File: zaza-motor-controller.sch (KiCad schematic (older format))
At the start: 74 parts, among them J1 VIN, J2 VIN, J3 CONN_02X05, J4 CONN_02X01, J5 GS3, Q1 3904, Q10 3906, Q11 3904, Q12 3904, Q2 3904, Q3 3906, Q4 3904, Q5 IXTA220, Q6 IXTA220, Q7 IXTA220, Q8 IXTA220, Q9 3904, U1 74HC00, U2 74HC00, U3 LM358, U4 LM555N

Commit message: Rev1 dev
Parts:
- removed D11, D12: BAT5H17, Diodes_SMD:D_MiniMELF_Standard, symbol D_Schottky_Small_ALT
- removed Q10: 3906, TO_SOT_Packages_SMD:SOT-23, symbol Q_PNP_BEC
- removed Q11, Q12, Q9: 3904, TO_SOT_Packages_SMD:SOT-23, symbol Q_NPN_BEC
- removed R10, R11, R13, R14: 10k, Resistors_SMD:R_0805, symbol R_Small
- removed R12: 47k, Resistors_SMD:R_0805, symbol R_Small
- removed R23: 3.3k, Resistors_SMD:R_0805, symbol R_Small
- added C15: CP, Capacitors_THT:CP_Axial_L29.0mm_D20.0mm_P35.00mm_Horizontal, symbol CP
- added C?: 220n, symbol C_Small
- added D? (x2): 15.6V, symbol D_Zener_Small_ALT
- added D? (x2): D, symbol D_Small_ALT
- added J?: MX120G, symbol CONN_02X06
- added MX120G: CONN_01X12, symbol CONN_01X12
- added Q?: Q_NPN_BCE, symbol Q_NPN_BCE
- added R? (x2): 10k, symbol R_Small
- added R?: 50R, symbol R_Small
- added R?: 10k, Resistors_SMD:R_0805, symbol R_Small
- added R? (x2): 1k, symbol R_Small
- added U?: 74xx595, symbol 74xx595
- added U?: 74xx138, symbol 74xx138
- added U?: LM7805CT, TO_SOT_Packages_THT:TO-220_Vertical, symbol LM7805CT
- added U?: IRS2003, symbol IRS2003
- Q1, Q2, Q4: value 3904 -> BC337
- Q3: value 3906 -> BC327
- R21: value 200k -> 180k
- R6: value 10k -> 100k
- R7: value 47k -> 0R
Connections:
- net +48V: now also R8.2, C15.1, MX120G.1 (P1), R?.1, R?.2; no longer Q3.3 (C), R8.1
- net +5V: now also U?.10 (R), U?.16, U?.16 (VCC), U?.6
- net GND: now also D?.2 (A), U?.13 (EN3), U?.2 (GND), U?.4, U?.5, U?.8, U?.8
- net GNDPWR: now also C15.2, MX120G.2 (P2), U?.4 (COM)
- net M+: now also R?.2
- net M-: now also C?.2, D?.2 (A), U?.6 (VS)
- net U: now also U?.15
- net V: now also U?.1
- net ~A: no longer R4.1
- net ~B: no longer R5.1
- net ~D: now also U?.2 (HIN)
- net at D10.1 (K), Q4.3 (C), Q6.1 (G)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: now also R8.1; no longer R8.2
- net at Q7.1 (G): now also R?.2
- net at Q8.1 (G): now also R?.2
- new net: Q3.3 (C), R?.1
- new net: D?.1 (K), Q?.1 (B), R?.1
- new net: Q?.2 (C), R?.2, R?.2
- new net: Q?.3 (E), U?.1 (IN)
- new net: R?.1, U?.5 (LO)
- new net: R?.1, U?.7 (HO)
- new net: C?.1, D?.1 (K), D?.1 (K), D?.1 (K), U?.8 (VB)
- new net: D?.2 (A), R?.1
- new net +15V: D?.2 (A), U?.1 (VCC)
- new net CS_ADDR0: MX120G.8 (P8), U?.1 (0)
- new net CS_ADDR1: MX120G.9 (P9), U?.2
- new net CS_ADDR2: MX120G.10 (P10), U?.3 (2)
- new net GNDREF: MX120G.4 (P4)
- new net MISO: MX120G.6 (P6)
- new net MOSI: MX120G.5 (P5), U?.14
- new net SCLK: MX120G.7 (P7), U?.11 (C1/->)
- new net ~CS_ADC: U?.13 (2)
- new net ~CS_DAC: U?.12 (3)
- new net ~CS_GPO: U?.12 (C2), U?.14 (1)
- no-connect marks 2 -> 15
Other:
- note added: "1\n1\n1\n1\n0"
- note added: "330mV/A"
- note added: "r_m = 10mV/A"
- note removed: "0\n0\n0\n0\n1"
- note removed: "V = 330mV/A"
- note removed: "rm = 10mV/A"
- moved on the sheet: C1, C10, C11, C12, C13, C14, C2, C3, C4, C5, C6, C7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

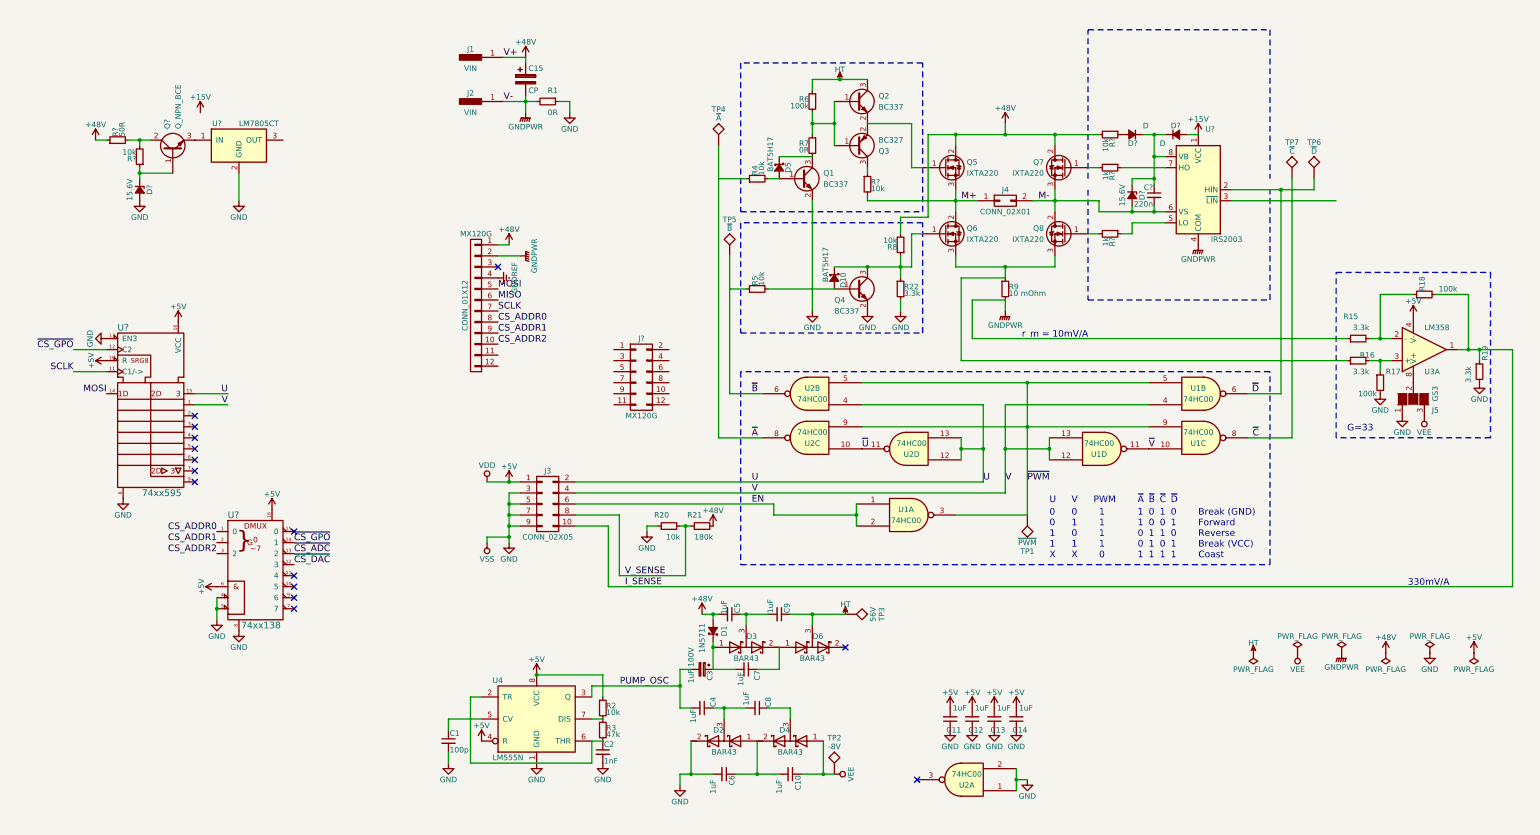
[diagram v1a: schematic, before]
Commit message: schematic: Getting closer to rev 1
Replace dscrete FET driver with IRS2003.
Add ADC, and other cool shit.
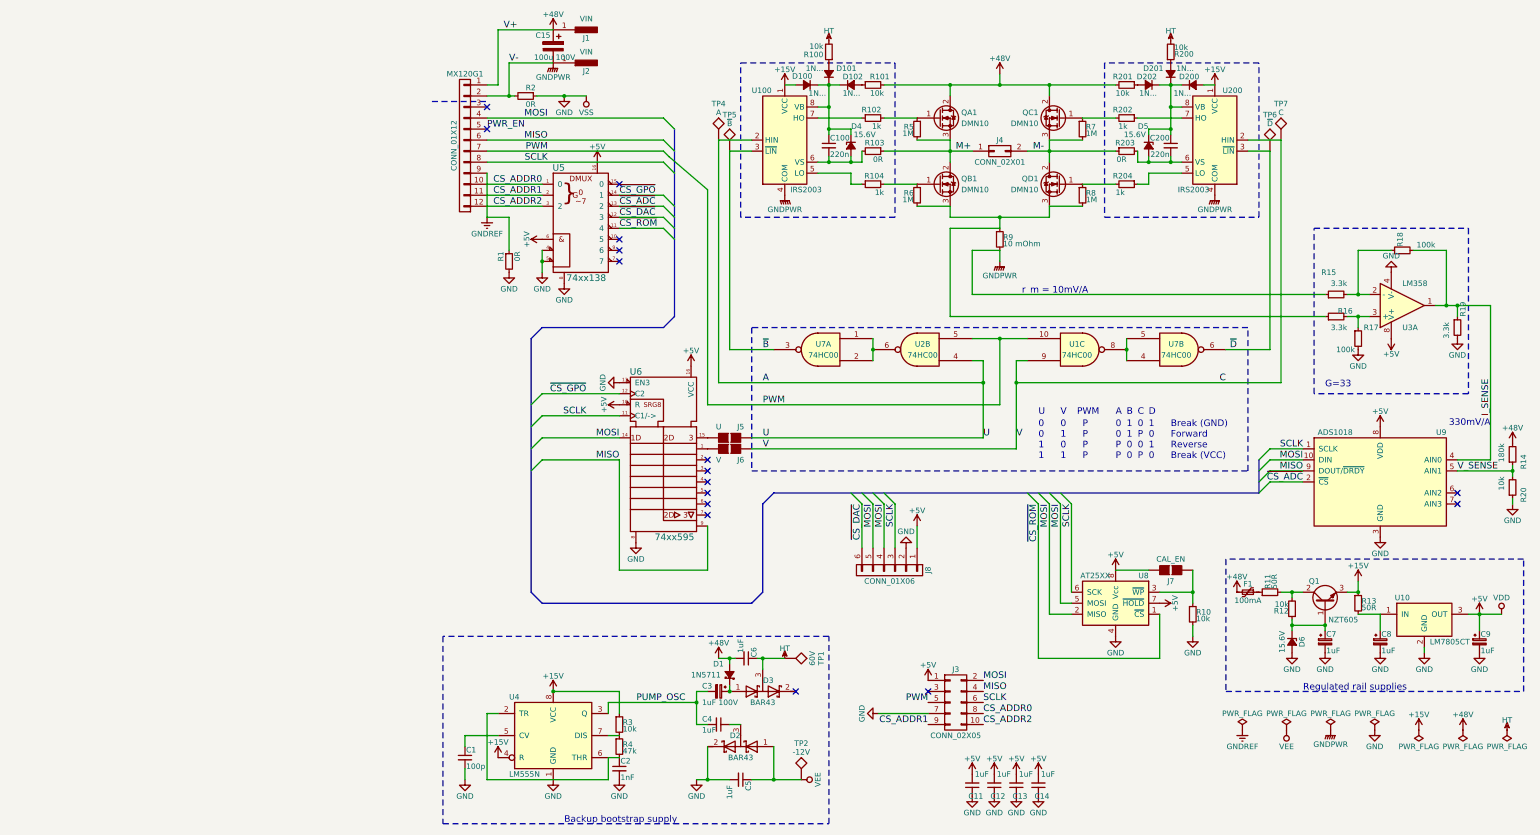
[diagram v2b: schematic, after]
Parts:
- removed C10, C7, C8, C9: 1uF, Capacitors_SMD:C_0805, symbol C_Small
- removed C?: 220n, symbol C_Small
- removed D10, D5: BAT5H17, Diodes_SMD:D_MiniMELF_Standard, symbol D_Schottky_Small_ALT
- removed D4, D6: BAR43, TO_SOT_Packages_SMD:SOT-23, symbol D_Schottky_x2_Serial_AKC
- removed D? (x2): D, symbol D_Small_ALT
- removed D?: 15.6V, symbol D_Zener_Small_ALT
- removed J5: GS3, Connectors:GS3, symbol GS3
- removed J?: MX120G, symbol CONN_02X06
- removed MX120G: CONN_01X12, symbol CONN_01X12
- removed Q1, Q2, Q4: BC337, TO_SOT_Packages_SMD:SOT-23, symbol Q_NPN_BEC
- removed Q3: BC327, TO_SOT_Packages_SMD:SOT-23, symbol Q_PNP_BEC
- removed R21: 180k, Resistors_SMD:R_0805, symbol R_Small
- removed R22: 3.3k, Resistors_SMD:R_0805, symbol R_Small
- removed R?: 10k, Resistors_SMD:R_0805, symbol R_Small
- removed R? (x2): 1k, symbol R_Small
- removed R?: 10k, symbol R_Small
- removed TP3: 56V, Measurement_Points:Test_Point_Keystone_5000-5004_Miniature, symbol TEST
- removed unit 3 of U1
- removed unit 4 of U1
- removed unit 1 of U1
- removed unit 3 of U2
- removed unit 4 of U2
- removed unit 1 of U2
- removed U?: IRS2003, symbol IRS2003
- added C100, C200: 220n, symbol C_Small
- added C7, C8, C9: 1uF, symbol CP_Small
- added D100, D101, D102, D200, D201, D202: 1N..., symbol D_Small_ALT
- added D4, D5: 15.6V, symbol D_Zener_Small_ALT
- added F1: 100mA, symbol Polyfuse_Small
- added J5: U, Connectors:GS2, symbol GS2
- added J6: V, Connectors:GS2, symbol GS2
- added J7: CAL_EN, Connectors:GS2, symbol GS2
- added J8: CONN_01X06, symbol CONN_01X06
- added MX120G1: CONN_01X12, symbol CONN_01X12
- added R10, R100, R101, R200, R201: 10k, symbol R_Small
- added R102, R104, R202, R204: 1k, symbol R_Small
- added R103, R203: 0R, symbol R_Small
- added R13: 50R, symbol R_Small
- added R14: 180k, Resistors_SMD:R_0805, symbol R_Small
- added U100, U200: IRS2003, symbol IRS2003
- added U7: 74HC00, Housings_SOIC:SOIC-14_3.9x8.7mm_Pitch1.27mm, symbol 74xx132
- added U8: AT25XX, symbol AT25_EEPROM
- added U9: ADS1018, symbol ADS1118I
- C15: value CP -> 100u 100V
- Q1: renamed from Q?; value Q_NPN_BCE -> NZT605
- QA1: renamed from Q5; value IXTA220 -> DMN10
- QB1: renamed from Q6; value IXTA220 -> DMN10
- QC1: renamed from Q7; value IXTA220 -> DMN10
- QD1: renamed from Q8; value IXTA220 -> DMN10
- R1: footprint Resistors_SMD:R_0805 -> (none)
- R2: value 10k -> 0R; footprint Resistors_SMD:R_0805 -> (none)
- R3: value 47k -> 10k
- R4: value 10k -> 47k
- R5, R8: value 10k -> 1M; footprint Resistors_SMD:R_0805 -> (none)
- R6: value 100k -> 1M; footprint Resistors_SMD:R_0805 -> (none)
- R7: value 0R -> 1M; footprint Resistors_SMD:R_0805 -> (none)
- TP1: value ~PWM -> 60V
- TP2: value -8V -> -12V
- TP4: value ~A -> A
- TP7: value ~C -> C
- gave numbers to parts that had none: 6
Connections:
- net EN is gone; now on net SCLK: J3.6 (P6)
- net +15V: now also Q1.3 (E), R3.1, U4.4 (R), U4.8 (VCC), D100.2 (A), D200.2 (A), R13.1, U100.1 (VCC), U200.1 (VCC)
- net +48V: now also C6.2, F1.2, MX120G1.1 (P1), R101.2, R14.2, R201.2; no longer C5.2, R11.1, R8.2
- net +5V: now also U10.3 (OUT), U3.8 (V+), C9.1, J7.1 (G1), J8.1 (P1), U7.14 (VDD), U7.14 (VDD), U8.7 (~HOLD), U8.8 (Vcc), U9.8 (VDD); no longer R2.1, U3.4 (V-), U4.4 (R), U4.8 (VCC)
- net CS_ADDR0: now also J3.8 (P8), MX120G1.10 (P10)
- net CS_ADDR1: now also J3.9 (P9), MX120G1.11 (P11)
- net CS_ADDR2: now also J3.10 (P10), MX120G1.12 (P12)
- net GND: now also C5.2, R1.2, R2.1, U3.4 (V-), C7.2, C8.2, C9.2, J8.2 (P2), R10.2, U7.7 (VSS), U7.7 (VSS), U8.4 (GND), U9.3 (GND); no longer C6.2, J3.3 (P3), J3.5 (P5), J3.9 (P9), R1.1
- net GNDPWR: now also R2.2, MX120G1.2 (P2), U100.4 (COM), U200.4 (COM); no longer R1.2
- net GNDREF: now also R1.1, MX120G1.9 (P9)
- net HT: now also C6.1, D3.3 (common), TP1.1, R100.2, R200.2; no longer R6.1
- net I_SENSE: now also U9.4 (AIN0); no longer J3.10 (P10)
- net M+: now also R5.2, R103.1
- net M-: now also R7.2, R203.1
- net MISO: now also J3.4 (P4), U6.9, MX120G1.6 (P6), U9.9 (DOUT/~DRDY)
- net MOSI: now also J3.2 (P2), J8.4 (P4), J8.5 (P5), MX120G1.4 (P4), U8.2 (MISO), U8.5 (MOSI), U9.10 (DIN)
- net SCLK: now also J8.3 (P3), MX120G1.8 (P8), U8.6 (SCK), U9.1 (SCLK)
- net VEE: now also C5.1, D2.1 (A)
- net V_SENSE: now also R14.1, U9.5 (AIN1); no longer J3.8 (P8)
- net ~B: now also U100.3 (~LIN), U7.3; no longer U2.6
- net ~CS_ADC: now also U9.2 (~CS)
- net ~CS_DAC: now also J8.6 (P6)
- net ~D: now also U200.3 (~LIN), U7.6; no longer U1.6
- net at QA1.1 (G): now also R5.1, R102.2
- net at QB1.1 (G): now also R6.1, R104.2; no longer R8.1
- net at QB1.3 (S), QD1.3 (S), R16.1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: now also R6.2, R8.2
- net at QC1.1 (G): now also R7.1, R202.2
- net at QD1.1 (G): now also R8.1, R204.2
- net at C2.1, U4.2 (TR), U4.6 (THR): now also R4.2; no longer R3.2
- net at R4.1: now also R3.2, U4.7 (DIS)
- net ~CS_ROM: now reaches U5.11 (4)
- net ~CS_ROM: now also U8.1 (~CS)
- net at D6.1 (K), Q1.1 (B), R12.1: now also C7.1
- net at U10.1 (IN): now also C8.1, R13.2; no longer Q1.3 (E)
- removed net U: J3.2 (P2), U2.4, U6.15
- removed net V: J3.4 (P4), U1.4, U6.1
- net ~A renamed A
- net A: now also U2.4, J5.1 (G1), U100.2 (HIN)
- net ~C renamed C
- net C: now also U1.9, J6.1 (G1), U200.2 (HIN)
- removed net ~PWM: TP1.1, U1.5, U2.5
- new net: U2.6, U7.1, U7.2
- new net: U1.8, U7.4, U7.5
- new net: J6.2 (G2), U6.1
- new net: J5.2 (G2), U6.15
- new net: F1.1, R11.1
- new net: R104.1, U100.5 (LO)
- new net: C100.2, D4.2 (A), R103.2, U100.6 (VS)
- new net: R102.1, U100.7 (HO)
- new net: C100.1, D100.1 (K), D101.1 (K), D102.1 (K), D4.1 (K), U100.8 (VB)
- new net: D102.2 (A), R101.1
- new net: D101.2 (A), R100.1
- new net: R204.1, U200.5 (LO)
- new net: C200.2, D5.2 (A), R203.2, U200.6 (VS)
- new net: R202.1, U200.7 (HO)
- new net: C200.1, D200.1 (K), D201.1 (K), D202.1 (K), D5.1 (K), U200.8 (VB)
- new net: D202.2 (A), R201.1
- new net: D201.2 (A), R200.1
- new net: J7.2 (G2), R10.1, U8.3 (~WP)
- new net PWM: J3.5 (P5), MX120G1.7 (P7), U1.10, U2.5
- new net PWR_EN: MX120G1.5 (P5)
- no-connect marks 15 -> 16
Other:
- note added: "0\n0\n1\n1"
- note added: "0\n0\nP\nP"
- note added: "0\n1\n0\n1"
- note added: "0\nP\n0\nP"
- note added: "1\n0\n1\n0"
- note added: "1\n1\n0\n0"
- note added: "A"
- note added: "B"
- note added: "Backup bootstrap supply"
- note added: "Break (GND)\nForward\nReverse\nBreak (VCC)"
- note added: "C"
- note added: "D"
- note added: "P\nP\nP\nP\n"
- note added: "Regulated rail supplies"
- note removed: "0\n0\n1\n1\n1"
- note removed: "0\n0\n1\n1\nX"
- note removed: "0\n1\n0\n1\n1"
- note removed: "0\n1\n0\n1\nX"
- note removed: "1\n0\n1\n0\n1"
- note removed: "1\n1\n0\n0\n1"
- note removed: "1\n1\n1\n1\n0"
- note removed: "Break (GND)\nForward\nReverse\nBreak (VCC)\nCoast"
- note removed: "~A"
- note removed: "~B"
- note removed: "~C"
- note removed: "~D"
- moved on the sheet: C11, C12, C13, C14, C15, D6, J1, J2, J3, J4, Q1, QA1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

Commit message: Incrase schematic chooch factor by warp 9
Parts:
- removed C4, C5: 1uF, Capacitors_SMD:C_0805, symbol C_Small
- removed D2: BAR43, TO_SOT_Packages_SMD:SOT-23, symbol D_Schottky_x2_Serial_AKC
- removed MX120G1: CONN_01X12, symbol CONN_01X12
- removed TP2: -12V, Measurement_Points:Test_Point_Keystone_5000-5004_Miniature, symbol TEST
- added J200: MX120G, symbol MX120G
- C1: value 100p -> 1n
- C100, C200, C7, C8, C9: footprint (none) -> Capacitors_SMD:C_0805
- C15: footprint Capacitors_THT:CP_Axial_L29.0mm_D20.0mm_P35.00mm_Horizontal -> Capacitors_THT:CP_Axial_L29.0mm_D16.0mm_P35.00mm_Horizontal
- C2: value 1nF -> 100p
- D100, D101, D102, D200, D201, D202: footprint (none) -> Diodes_SMD:D_MiniMELF_Standard
- D103: renamed from D4; footprint (none) -> Diodes_SMD:D_SOD-323
- D203: renamed from D5; footprint (none) -> Diodes_SMD:D_SOD-323
- D6: footprint (none) -> Diodes_SMD:D_SOD-323
- F1: footprint (none) -> Resistors_SMD:R_1206
- J3: footprint Connectors:IDC_Header_Straight_10pins -> Connectors_Multicomp:Multicomp_MC9A12-1034_2x05x2.54mm_Straight
- J5, J6, J7: footprint Connectors:GS2 -> Pin_Headers:Pin_Header_Straight_2x01_Pitch2.54mm
- J8: footprint (none) -> Pin_Headers:Pin_Header_Straight_1x06_Pitch2.54mm
- Q1: footprint (none) -> TO_SOT_Packages_SMD:SOT-223-3Lead_TabPin2
- R1, R10, R100, R101, R102, R103, R104, R12, R2, R200, R201, R202, R203, R204, R5, R6, R7, R8: footprint (none) -> Resistors_SMD:R_0805
- R11, R13: footprint (none) -> Resistors_SMD:R_2010
- U10: footprint TO_SOT_Packages_THT:TO-220_Vertical -> TO_SOT_Packages_SMD:SOT-223-3Lead_TabPin2
- U100, U200, U8: footprint (none) -> Housings_SOIC:SOIC-8_3.9x4.9mm_Pitch1.27mm
- U5, U6: footprint (none) -> Housings_SOIC:SOIC-16_3.9x9.9mm_Pitch1.27mm
- U9: footprint (none) -> Housings_SSOP:MSOP-10_3x3mm_Pitch0.5mm
- renumbered U2 to U1, U7 to U1
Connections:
- net +48V: now also J200.1 (P1)
- net A: now also U1.2; no longer U1.4
- net C: now also U1.13; no longer U1.9
- net CS_ADDR0: now also J200.11 (P11)
- net CS_ADDR1: now also J200.6 (P6)
- net CS_ADDR2: now also J200.12 (P12)
- net GND: no longer C1.2, C2.2, C7.2, D6.2 (A), U4.1 (GND)
- net GNDPWR: now also C1.2, C2.2, C7.2, D6.2 (A), U4.1 (GND), J200.7 (P7)
- net GNDREF: now also J200.5 (P5)
- net MISO: now also J200.9 (P9); no longer U6.9
- net MOSI: now also J200.8 (P8)
- net PWM: now also U1.1, U1.12, J200.4 (P4); no longer U1.10, U1.5
- net PWR_EN: now also J200.3 (P3)
- net SCLK: now also J200.10 (P10)
- net ~B: now also U1.6; no longer U1.3
- net ~D: now also U1.8; no longer U1.6
- new net: U1.3, U1.4, U1.5
- new net: U1.10, U1.11, U1.9
- no-connect marks 16 -> 17
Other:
- note added: "PWM modulation logic"
- moved on the sheet: C3, C6, D1, D3, J3, TP1
